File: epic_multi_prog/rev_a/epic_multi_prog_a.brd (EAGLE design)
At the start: 61 x 35.6 mm, 28 parts, among them J1 EPIC-PROG-PORT, J2 MICRO_USB_B_HIROSE_ZX62R-B-5P, J3 MEC1-105-02-XX-XX-D-A, J4 TAG_CONNECT_HEADER_EPIC, U1 FT232RL, U2 MAX1555

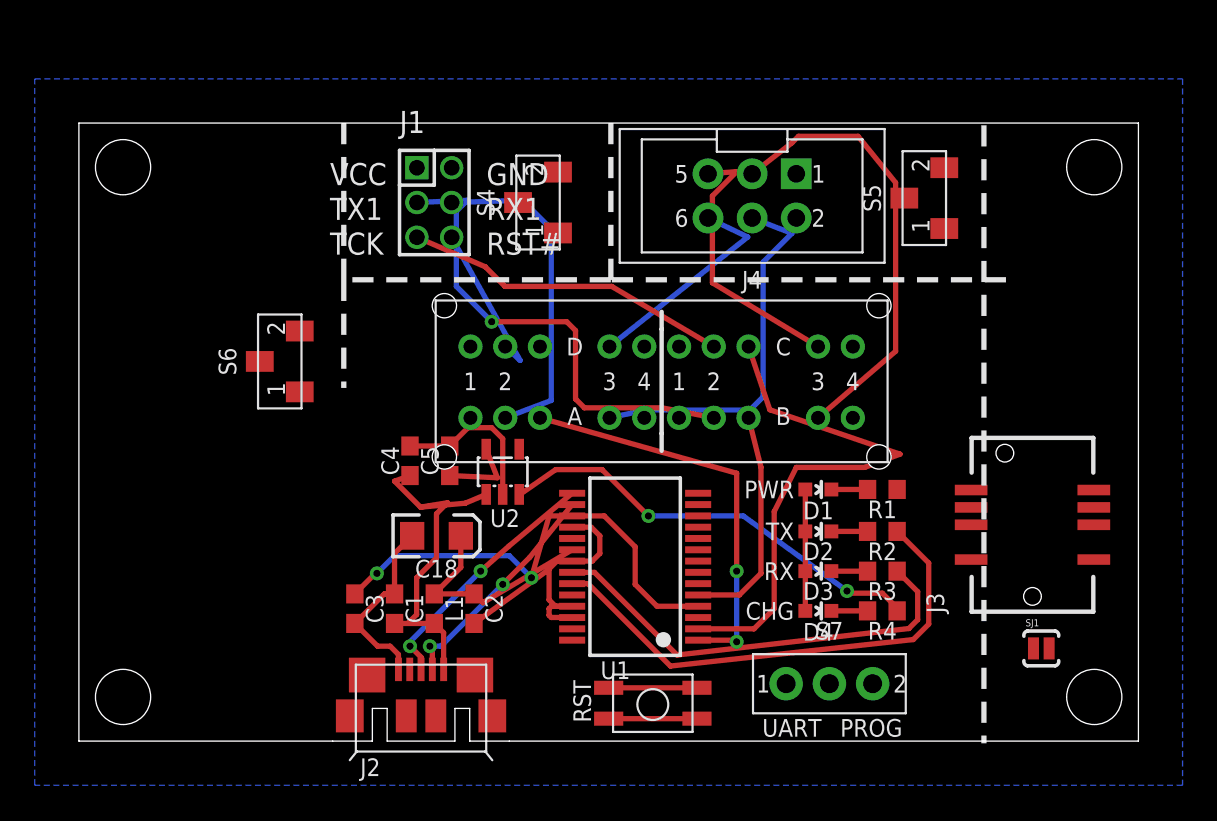
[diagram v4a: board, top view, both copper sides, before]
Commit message: Nearly routed, added more max1555s
Decided that each circuit should have its own charging led.
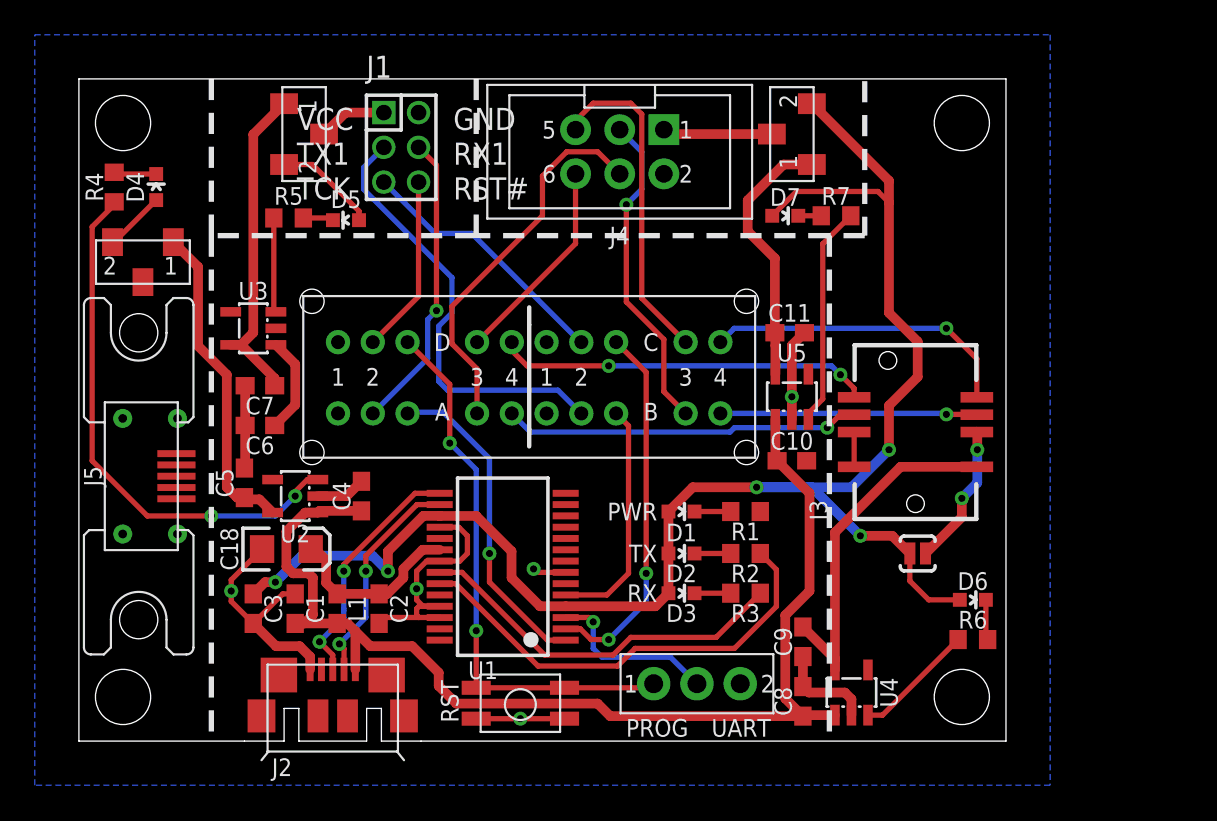
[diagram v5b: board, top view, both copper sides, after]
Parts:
- added C10, C11, C6, C7, C8, C9: 1u, rcl:C0603
- added D5, D6, D7: YELLOW, SparkFun:LED-0603
- added J5: MICRO_USB_B_MALE_HIROSE_ZX80-B-5S, connector:USB_MICRO_B_MALE-HIROSE-ZX80-B-5S
- added R5, R6, R7: 470, rcl:R0603
- added U3, U4, U5: MAX1555, maxim:SOT23-5L
- moved R4 50.5 mm to (2.03, 31.9), turned to 270 degrees
- moved D4 45.2 mm to (4.45, 31.9), turned to 0 degrees
- moved S4 14.0 mm to (13.0, 34.9), turned to 270 degrees
- moved U2 12.0 mm to (12.4, 14.1), turned to 90 degrees
- moved C5 11.9 mm to (9.53, 14.9)
- moved S6 9.73 mm to (3.68, 27.6), turned to 180 degrees
- moved SJ1 8.97 mm to (48.3, 10.8)
- moved C18 8.67 mm to (11.9, 11.0)
- moved J3 8.59 mm to (48.1, 17.8)
- moved S5 8.46 mm to (41.0, 34.9)
- moved J4 8.03 mm to (31.1, 33.9)
- moved D1 7.98 mm to (34.7, 13.2)
- moved D2 7.98 mm to (34.7, 10.8)
- moved D3 7.98 mm to (34.7, 8.51)
- moved R1 7.98 mm to (38.4, 13.2)
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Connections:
- removed net BATT_CHG: C5.1, J3.1, S4.1, S5.1, S6.1, U2.5
- new net BATT_CHG_EDGE: C9.1, J3.1, U4.5
- new net BATT_CHG_MINIPROG: C7.1, S4.1, U3.5
- new net BATT_CHG_OPO: C5.1, S6.1, U2.5
- new net BATT_CHG_POGO: C11.1, S5.1, U5.5
- new net N$14: J5.3
- new net N$15: J5.4
- new net N$16: R5.2, U3.3
- new net N$17: J5.SHIELD1, J5.SHIELD2, J5.SHIELD3, J5.SHIELD4
- new net N$18: D6.C, R6.1
- new net N$19: R6.2, U4.3
- new net N$20: D7.C, R7.1
- new net N$21: R7.2, U5.3
- new net N$5: D5.C, R5.1
- net !RST: now also S7.1; no longer S7.2
- net 3V3: now also D5.A, D6.A, D7.A
- net GND: now also C10.2, C11.2, C6.2, C7.2, C8.2, C9.2, J5.5, U3.2, U4.2, U5.2
- net N$13: now also J5.2; no longer S7.1
- net USB5V: now also C10.1, C6.1, C8.1, U3.1, U4.1, U5.1
- net VCC_OPO: now also J5.1
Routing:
- net 3V3: track 34.3 -> 104.8 mm, vias 2 -> 5
- net USB5V: track 21.6 -> 71.9 mm
- net !RST: track 5.08 -> 31.8 mm, vias 0 -> 2
- net !RST_EDGE: track 0.00 -> 21.6 mm, vias 0 -> 2
- net RX_EDGE: track 0.00 -> 20.6 mm, vias 0 -> 1
- net BATT_CHG_EDGE: track 0.00 -> 20.2 mm
- net BATT_CHG_MINIPROG: track 0.00 -> 18.7 mm
- net BATT_CHG_OPO: track 0.00 -> 18.6 mm
- net TCK_EDGE: track 0.00 -> 18.0 mm, vias 0 -> 1
- net BATT_CHG_POGO: track 0.00 -> 15.2 mm
- net TX_EDGE: track 0.00 -> 14.8 mm, vias 0 -> 1
- net N$21: track 0.00 -> 12.7 mm
- net GND: track 43.4 -> 56.0 mm, vias 0 -> 5
- net !RST_USB: track 0.00 -> 10.0 mm, vias 0 -> 1
- net TCK: track 31.1 -> 21.5 mm, vias 0 -> 2
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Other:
- board size 61 x 35.6 mm -> 53.3 x 38.1 mm
- board text removed: "CHG"

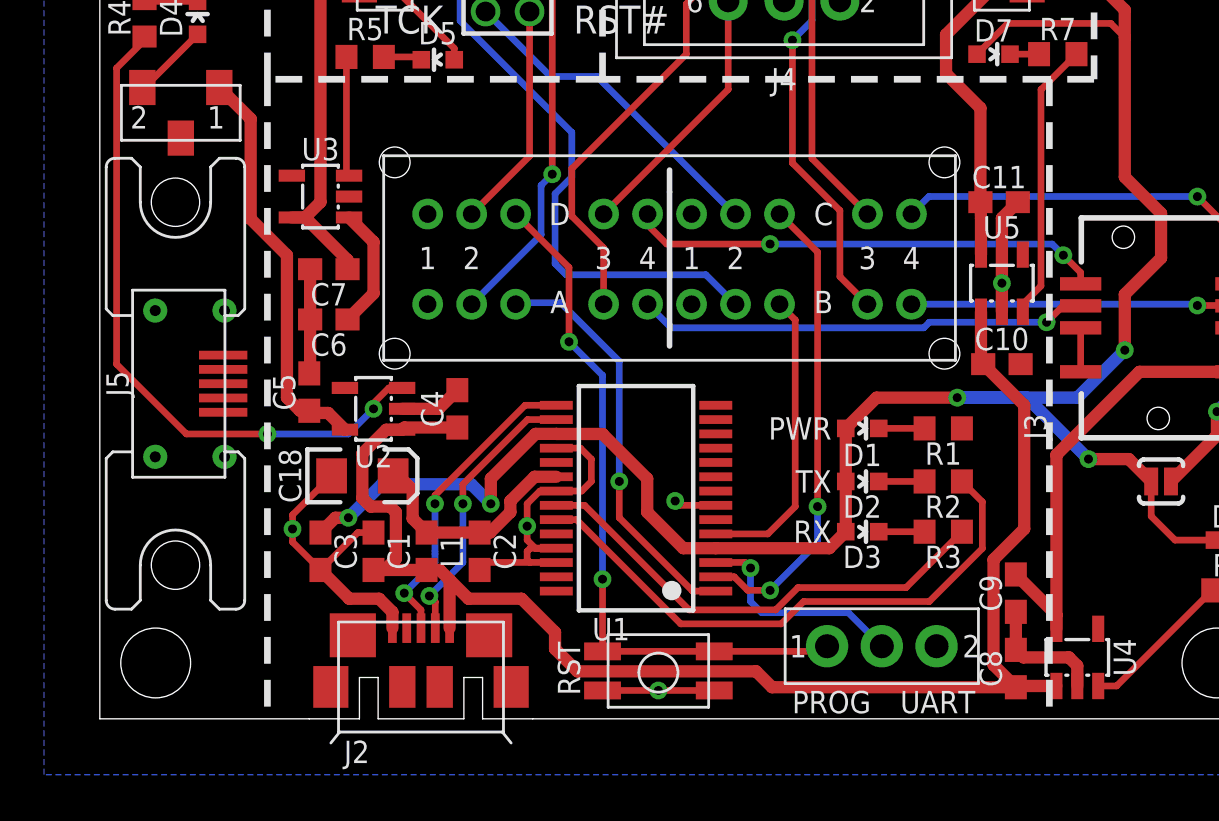
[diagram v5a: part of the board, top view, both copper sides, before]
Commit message: Cleaned up airwires
Need to get the pinout for programming opo.
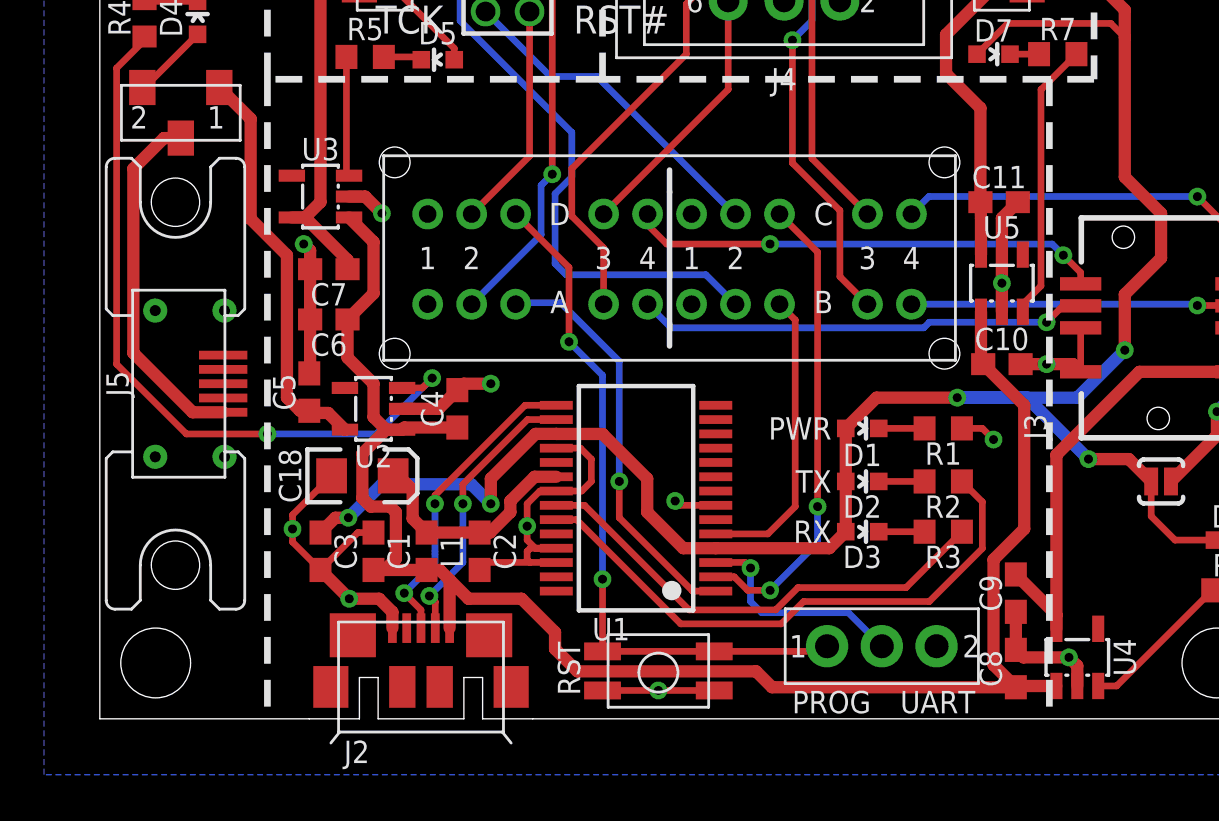
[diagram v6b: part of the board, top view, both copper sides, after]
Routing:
- net VCC_OPO: track 0.00 -> 16.3 mm
- net GND: track 56.0 -> 65.2 mm, vias 5 -> 12
- net USB5V: track 71.9 -> 77.6 mm
- net N$12: track 31.1 -> 34.0 mm
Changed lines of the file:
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@@
 <wire x1="12.7" y1="5.461" x2="11.342" y2="5.461" width="0.5588" layer="1"/>
 <wire x1="11.342" y1="5.461" x2="10.033" y2="6.77" width="0.5588" layer="1"/>
-<wire x1="22.86" y1="1.289" x2="27.94" y2="1.289" width="0.3048" layer="1"/>
 <wire x1="20.759" y1="7.758" x2="19.569" y2="7.758" width="0.3048" layer="1"/>
 <wire x1="19.569" y1="7.758" x2="19.431" y2="7.62" width="0.3048" layer="1"/>
@@
 <wire x1="9.525" y1="15.709" x2="9.564" y2="15.875" width="0.5588" layer="1"/>
 <wire x1="9.564" y1="15.875" x2="9.564" y2="18.161" width="0.5588" layer="1"/>
-<wire x1="41.871" y1="16.129" x2="44.603" y2="15.78" width="0" layer="19" extent="1-1"/>
-<wire x1="41.021" y1="18.512" x2="41.871" y2="16.129" width="0" layer="19" extent="1-1"/>
-<wire x1="8.763" y1="8.04" x2="8.763" y2="8.636" width="0" layer="19" extent="1-1"/>
-<wire x1="27.94" y1="1.289" x2="25.4" y2="1.289" width="0" layer="19" extent="1-1"/>
-<wire x1="39.204" y1="13.208" x2="41.871" y2="16.129" width="0" layer="19" extent="1-1"/>
-<wire x1="13.746" y1="14.097" x2="10.538" y2="11.049" width="0" layer="19" extent="1-1"/>
-<wire x1="9.525" y1="15.709" x2="13.746" y2="14.097" width="0" layer="19" extent="1-1"/>
-<wire x1="11.333" y1="23.749" x2="9.564" y2="20.447" width="0" layer="19" extent="1-1"/>
-<wire x1="5.61" y1="16.54" x2="9.525" y2="15.709" width="0" layer="19" extent="1-1"/>
-<wire x1="41.656" y1="4.865" x2="39.204" y2="13.208" width="0" layer="19" extent="1-1"/>
+<via x="44.069" y="2.794" extent="1-16" drill="0.4064"/>
+<wire x1="41.871" y1="16.129" x2="43.053" y2="16.129" width="0.5588" layer="1"/>
+<wire x1="43.053" y1="16.129" x2="44.254" y2="16.129" width="0.5588" layer="1"/>
+<wire x1="44.254" y1="16.129" x2="44.603" y2="15.78" width="0.5588" layer="1"/>
+<via x="43.053" y="16.129" extent="1-16" drill="0.4064"/>
+<wire x1="39.204" y1="13.208" x2="40.132" y2="13.208" width="0.3048" layer="1"/>
+<wire x1="40.132" y1="13.208" x2="40.64" y2="12.7" width="0.3048" layer="1"/>
+<via x="40.64" y="12.7" extent="1-16" drill="0.4064"/>
+<wire x1="16.256" y1="14.947" x2="16.549" y2="15.24" width="0.5588" layer="1"/>
+<wire x1="16.549" y1="15.24" x2="17.78" y2="15.24" width="0.5588" layer="1"/>
+<via x="17.78" y="15.24" extent="1-16" drill="0.4064"/>
+<via x="11.342" y="5.461" extent="1-16" drill="0.4064"/>
+<wire x1="11.333" y1="23.749" x2="12.065" y2="23.749" width="0.5588" layer="1"/>
+<wire x1="12.065" y1="23.749" x2="12.827" y2="22.987" width="0.5588" layer="1"/>
+<via x="12.827" y="22.987" extent="1-16" drill="0.4064"/>
+<wire x1="9.564" y1="20.447" x2="9.564" y2="21.297" width="0.5588" layer="1"/>
+<wire x1="9.564" y1="21.297" x2="9.271" y2="21.59" width="0.5588" layer="1"/>
+<via x="9.271" y="21.59" extent="1-16" drill="0.4064"/>
+<wire x1="27.94" y1="1.289" x2="25.4" y2="1.289" width="0.3048" layer="1"/>
+<wire x1="22.86" y1="1.289" x2="25.4" y2="1.289" width="0.3048" layer="1"/>
+<wire x1="9.525" y1="15.709" x2="5.61" y2="16.54" width="0" layer="19" extent="1-1"/>
 </signal>
 <signal name="USB5V">
@@
 <wire x1="13.746" y1="13.147" x2="13.846" y2="13.247" width="0.5588" layer="1"/>
 <wire x1="13.846" y1="13.247" x2="16.256" y2="13.247" width="0.5588" layer="1"/>
-<wire x1="13.02" y1="13.147" x2="11.264" y2="18.161" width="0" layer="19" extent="1-1"/>
+<wire x1="11.264" y1="18.161" x2="11.264" y2="16.422" width="0.5588" layer="1"/>
+<wire x1="11.264" y1="16.422" x2="12.446" y2="15.24" width="0.5588" layer="1"/>
+<wire x1="12.446" y1="15.24" x2="12.446" y2="13.721" width="0.5588" layer="1"/>
+<wire x1="12.446" y1="13.721" x2="13.02" y2="13.147" width="0.5588" layer="1"/>
 </signal>
 <signal name="N$3">
@@
 <wire x1="41.287" y1="31.623" x2="45.974" y2="31.623" width="0.3048" layer="1"/>
 <wire x1="45.974" y1="31.623" x2="46.609" y2="30.988" width="0.3048" layer="1"/>
-<wire x1="4.445" y1="31.127" x2="11.804" y2="33.175" width="0" layer="19" extent="1-1"/>
-<wire x1="19.816" y1="12.958" x2="16.117" y2="29.972" width="0" layer="19" extent="1-1"/>
 <wire x1="1.933" y1="28.709" x2="2.027" y2="28.709" width="0.3048" layer="1"/>
 <wire x1="2.027" y1="28.709" x2="4.445" y2="31.127" width="0.3048" layer="1"/>
@@
 <wire x1="48.26" y1="22.987" x2="46.609" y2="24.638" width="0.5588" layer="1"/>
 <wire x1="46.609" y1="24.638" x2="46.609" y2="30.988" width="0.5588" layer="1"/>
+<wire x1="4.445" y1="31.127" x2="11.804" y2="33.175" width="0" layer="19" extent="1-1"/>
+<wire x1="19.816" y1="12.958" x2="16.117" y2="29.972" width="0" layer="19" extent="1-1"/>
 </signal>
 <signal name="!RST">
@@
 <wire x1="2.032" y1="30.861" x2="2.032" y2="31.027" width="0.3048" layer="1"/>
 <wire x1="13.746" y1="15.047" x2="13.396" y2="15.047" width="0.3048" layer="1"/>
-<via x="12.446" y="14.097" extent="1-16" drill="0.4064"/>
-<wire x1="12.446" y1="14.097" x2="11.303" y2="12.954" width="0.3048" layer="16"/>
-<wire x1="11.303" y1="12.954" x2="7.62" y2="12.954" width="0.3048" layer="16"/>
-<wire x1="12.446" y1="14.097" x2="12.446" y2="14.351" width="0.3048" layer="1"/>
-<wire x1="12.446" y1="14.351" x2="13.142" y2="15.047" width="0.3048" layer="1"/>
-<wire x1="13.142" y1="15.047" x2="13.746" y2="15.047" width="0.3048" layer="1"/>
+<wire x1="12.573" y1="12.954" x2="7.62" y2="12.954" width="0.3048" layer="16"/>
+<wire x1="13.746" y1="15.047" x2="14.666" y2="15.047" width="0.3048" layer="1"/>
+<wire x1="14.666" y1="15.047" x2="15.113" y2="15.494" width="0.3048" layer="1"/>
+<via x="15.113" y="15.494" extent="1-16" drill="0.4064"/>
+<wire x1="15.113" y1="15.494" x2="12.573" y2="12.954" width="0.3048" layer="16"/>
 </signal>
 <signal name="TCK_EDGE">
@@
 <contactref element="S6" pad="IN"/>
 <contactref element="J5" pad="1"/>
-<wire x1="5.61" y1="13.94" x2="3.683" y2="26.409" width="0" layer="19" extent="1-1"/>
+<wire x1="3.683" y1="26.409" x2="2.914" y2="26.409" width="0.5588" layer="1"/>
+<wire x1="2.914" y1="26.409" x2="1.524" y2="25.019" width="0.5588" layer="1"/>
+<wire x1="1.524" y1="25.019" x2="1.524" y2="16.637" width="0.5588" layer="1"/>
+<wire x1="1.524" y1="16.637" x2="4.221" y2="13.94" width="0.5588" layer="1"/>
+<wire x1="4.221" y1="13.94" x2="5.61" y2="13.94" width="0.5588" layer="1"/>
 </signal>
 <signal name="N$13">

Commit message: added opo usb connection
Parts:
- renumbered C18 to C12, S7 to S1
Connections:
- removed net N$13: J5.2
- removed net N$14: J5.3
- removed net N$15: J5.4
- removed net N$17: J5.SHIELD1, J5.SHIELD2, J5.SHIELD3, J5.SHIELD4
- net !RST_OPO: now also J5.5
- net GND: now also J5.SHIELD1, J5.SHIELD2, J5.SHIELD3, J5.SHIELD4; no longer J5.5
- net RX_OPO: now also J5.3
- net TCK_OPO: now also J5.4
- net TX_OPO: now also J5.2
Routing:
- net TCK_OPO: track 0.00 -> 34.4 mm, vias 0 -> 2
- net TX_OPO: track 0.00 -> 23.7 mm, vias 0 -> 2
- net !RST_OPO: track 0.00 -> 12.0 mm, vias 0 -> 1
- net RX_OPO: track 0.00 -> 10.8 mm, vias 0 -> 1
- net !RST_POGO: track 12.0 -> 15.1 mm
- net TX_MINIPROG: track 25.3 -> 27.9 mm
- net N$12: track 34.0 -> 36.5 mm
- net RX_POGO: track 22.0 -> 24.3 mm
